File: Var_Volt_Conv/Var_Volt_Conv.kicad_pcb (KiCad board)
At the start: 6 copper layers, 114 x 120 mm, 98 parts, among them J101 Jack-DC, J102 Screw_Terminal_01x02, J103 Screw_Terminal_01x02, J201 Conn_01x05, Q101 AO3416, Q102 IRFML8244TRPBF, Q103 IRFML8244TRPBF, Q104 AO3407, Q105 AO3407, Q106 AO3407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

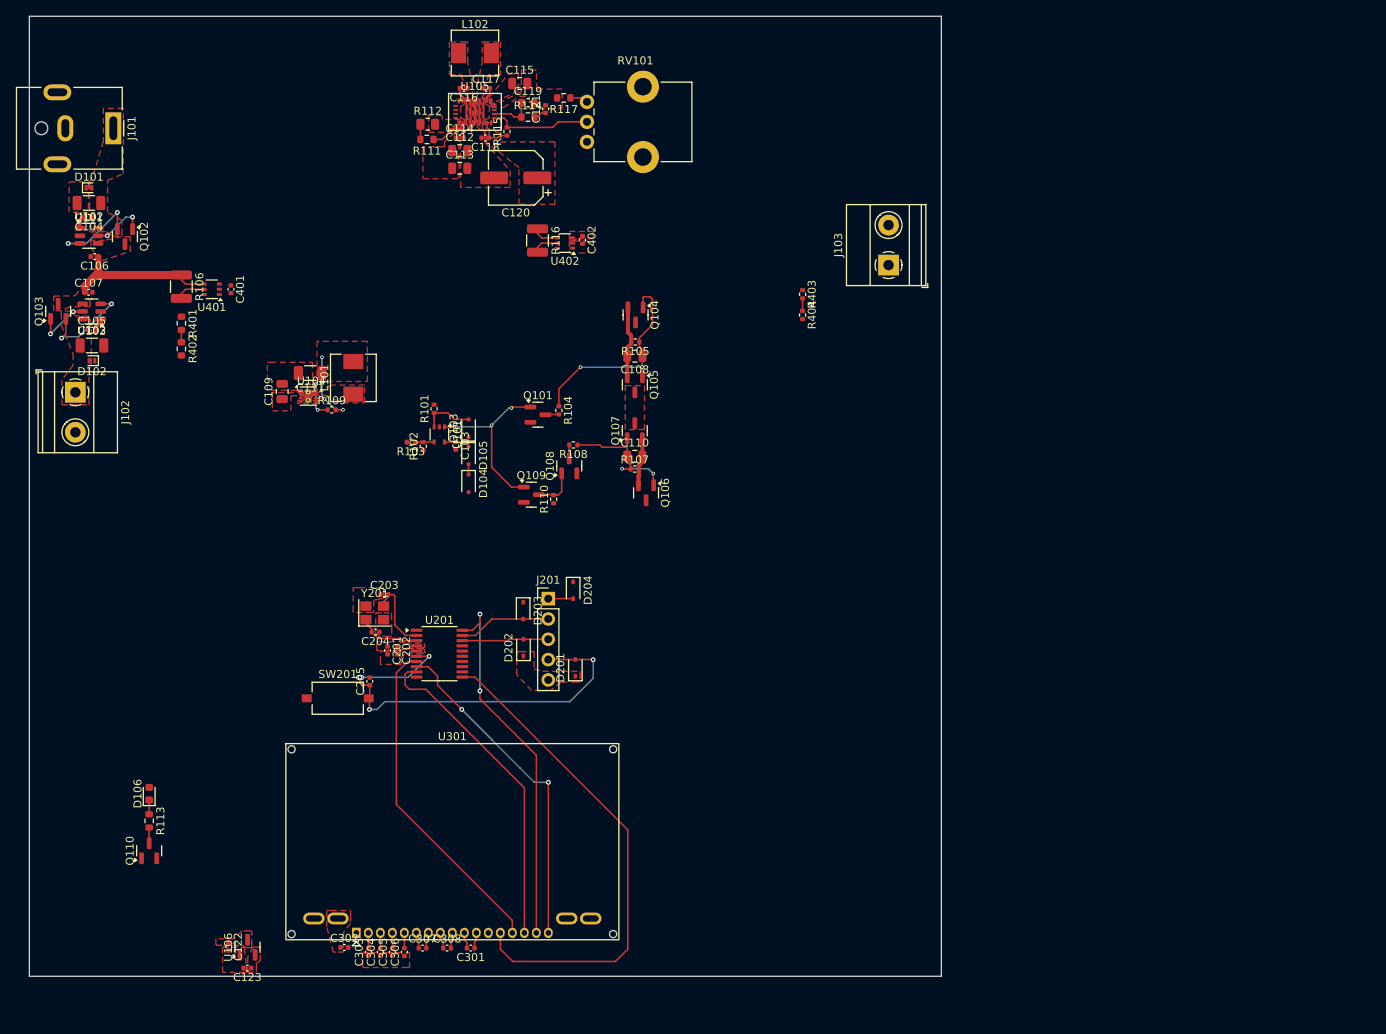
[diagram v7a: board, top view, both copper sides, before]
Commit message: Rounded PCB corners and add remaining 3D models
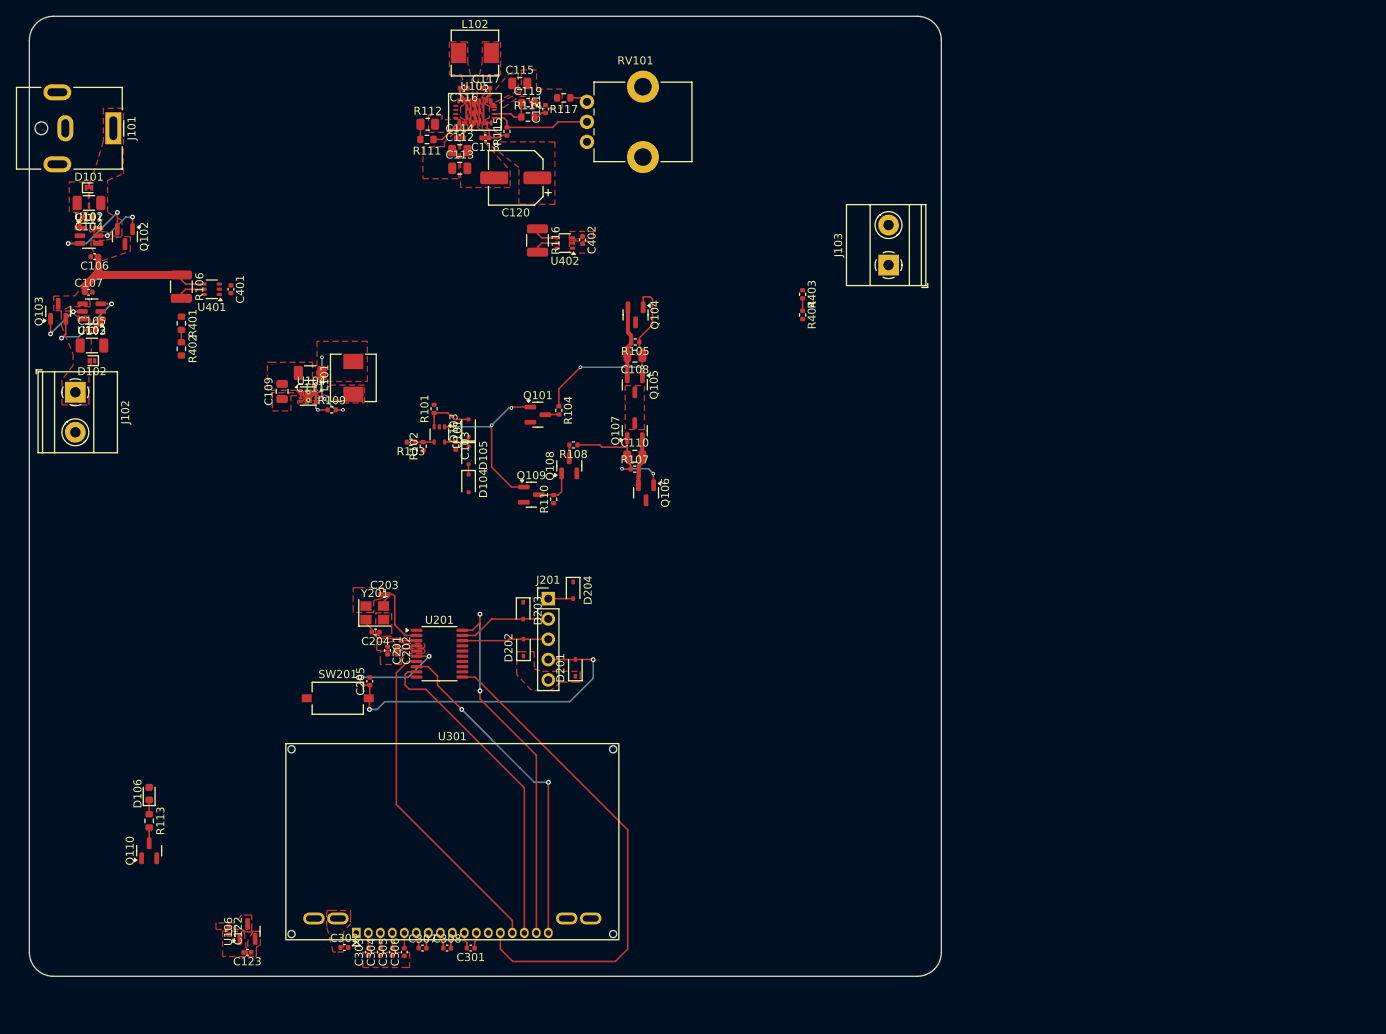
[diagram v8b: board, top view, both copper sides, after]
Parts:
- moved C122 1.98 mm to (44.9, 134.3)
- moved C123 1.97 mm to (47.2, 137.0)
- moved U106 1.97 mm to (47.3, 134.4)
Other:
- outline, holes or cut-outs redrawn
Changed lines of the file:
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@@
 			(remove_unused_layers no)
 		)
-		(model "${KICAD8_3DMODEL_DIR}/Display.3dshapes/NHD-C12832A1Z-FSRGB.wrl"
+		(model "${KIPRJMOD}/Project_Library/3d_Models/NHD-C12832A1Z.STEP"
 			(offset
-				(xyz 0 0 0)
+				(xyz 12 11.5 0)
 			)
 			(scale
@@
 	(footprint "Package_TO_SOT_SMD:SOT-23"
 		(layer "F.Cu")
-		(at 47.275 136.375 90)
+		(at 47.275 134.4 90)
 		(descr "SOT, 3 Pin (https://www.jedec.org/system/files/docs/to-236h.pdf variant AB), generated with kicad-footprint-generator ipc_gullwing_generator.py")
 		(tags "SOT TO_SOT_SMD")
@@
 		(tags "resistor")
 		(property "Reference" "R117"
-			(at 0 -1.43 360)
+			(at 0 -1.43 0)
 			(layer "F.SilkS")
 			(effects
@@
 		)
 		(property "Value" "6.4k"
-			(at 0 1.43 360)
+			(at 0 1.43 0)
 			(layer "F.Fab")
 			(effects
@@
 		)
 		(fp_text user "${REFERENCE}"
-			(at 0 0 360)
+			(at 0 0 0)
 			(layer "F.Fab")
 			(effects
@@
 			(pintype "passive")
 		)
-		(model "${KICAD8_3DMODEL_DIR}/Potentiometer_THT.3dshapes/Potentiometer_Bourns_PTV09A-1_Single_Vertical.wrl"
+		(model "${KIPRJMOD}/Project_Library/3d_Models/PTV09A-4225F-B104.step"
 			(offset
-				(xyz 0 0 0)
+				(xyz 7 2.5 0)
 			)
 			(scale
@@
 			)
 			(rotate
-				(xyz 0 0 0)
+				(xyz -90 0 90)
 			)
 		)
@@
 		(tags "SOT-363 SC-70-6")
 		(property "Reference" "U402"
-			(at 0 -2.25 360)
+			(at 0 -2.25 0)
 			(layer "F.SilkS")
 			(effects
@@
 		)
 		(property "Value" "INA215BIDCKR"
-			(at 0 2 360)
+			(at 0 2 0)
 			(layer "F.Fab")
 			(effects
@@
 		(tags "resistor")
 		(property "Reference" "R112"
-			(at 0 -1.65 360)
+			(at 0 -1.65 0)
 			(layer "F.SilkS")
 			(effects
@@
 		)
 		(property "Value" "4.3k"
-			(at 0 1.65 360)
+			(at 0 1.65 0)
 			(layer "F.Fab")
 			(effects
@@
 		)
 		(fp_text user "${REFERENCE}"
-			(at 0 0 360)
+			(at 0 0 0)
 			(layer "F.Fab")
 			(effects
@@
 		(tags "resistor")
 		(property "Reference" "R105"
-			(at 0 -1.17 360)
+			(at 0 -1.17 0)
 			(layer "F.SilkS")
 			(effects
@@
 		)
 		(property "Value" "100k"
-			(at 0 1.17 360)
+			(at 0 1.17 0)
 			(layer "F.Fab")
 			(effects
@@
 		)
 		(fp_text user "${REFERENCE}"
-			(at 0 0 360)
+			(at 0 0 0)
 			(layer "F.Fab")
 			(effects
@@
 	(footprint "Capacitor_SMD:C_0402_1005Metric"
 		(layer "F.Cu")
-		(at 47.25 138.975 180)
+		(at 47.25 137 180)
 		(descr "Capacitor SMD 0402 (1005 Metric), square (rectangular) end terminal, IPC_7351 nominal, (Body size source: IPC-SM-782 page 76, https://www.pcb-3d.com/wordpress/wp-content/uploads/ipc-sm-782a_amendment_1_and_2.pdf), generated with kicad-footprint-generator")
 		(tags "capacitor")
@@
 		(tags "capacitor")
 		(property "Reference" "C108"
-			(at 0 -1.68 360)
+			(at 0 -1.68 0)
 			(layer "F.SilkS")
 			(effects
@@
 		)
 		(property "Value" "10uF"
-			(at 0 1.68 360)
+			(at 0 1.68 0)
 			(layer "F.Fab")
 			(effects
@@
 		)
 		(fp_text user "${REFERENCE}"
-			(at 0 0 360)
+			(at 0 0 0)
 			(layer "F.Fab")
 			(effects
@@
 	(footprint "Capacitor_SMD:C_0402_1005Metric"
 		(layer "F.Cu")
-		(at 44.925 136.3 -90)
+		(at 44.925 134.325 -90)
 		(descr "Capacitor SMD 0402 (1005 Metric), square (rectangular) end terminal, IPC_7351 nominal, (Body size source: IPC-SM-782 page 76, https://www.pcb-3d.com/wordpress/wp-content/uploads/ipc-sm-782a_amendment_1_and_2.pdf), generated with kicad-footprint-generator")
 		(tags "capacitor")
@@
 		)
 	)
+	(gr_arc
+		(start 20 23)
+		(mid 20.87868 20.87868)
+		(end 23 20)
+		(stroke
+			(width 0.05)
+			(type default)
+		)
+		(layer "Edge.Cuts")
+	)
+	(gr_arc
+		(start 134 137)
+		(mid 133.12132 139.12132)
+		(end 131 140)
+		(stroke
+			(width 0.05)
+			(type default)
+		)
+		(layer "Edge.Cuts")
+	)
 	(gr_line
-		(start 134 140)
-		(end 20 140)
+		(start 131 140)
+		(end 23 140)
+		(stroke
+			(width 0.05)
+			(type default)
+		)
+		(layer "Edge.Cuts")
+	)
+	(gr_arc
+		(start 23 140)
+		(mid 20.87868 139.12132)
+		(end 20 137)
+		(stroke
+			(width 0.05)
+			(type default)
+		)
+		(layer "Edge.Cuts")
+	)
+	(gr_arc
+		(start 131 20)
+		(mid 133.12132 20.87868)
+		(end 134 23)
 		(stroke
 			(width 0.05)
@@
 	)
 	(gr_line
-		(start 134 20)
-		(end 134 140)
+		(start 134 23)
+		(end 134 137)
 		(stroke
 			(width 0.05)
@@
 	)
 	(gr_line
-		(start 20 20)
-		(end 134 20)
+		(start 23 20)
+		(end 131 20)
 		(stroke
 			(width 0.05)
@@
 	)
 	(gr_line
-		(start 20 140)
-		(end 20 20)
+		(start 20 137)
+		(end 20 23)
 		(stroke
 			(width 0.05)
@@
 		(polygon
 			(pts
-				(xy 44.15 136.35) (xy 46.875 136.35) (xy 46.875 136.525) (xy 47.125 138.7) (xy 47.125 139.525) (xy 46.95 139.525)
-				(xy 44.575 139.5) (xy 44.325 139.5) (xy 44.15 139.5) (xy 44.15 136.475)
+				(xy 44.15 134.375) (xy 46.875 134.375) (xy 46.875 134.55) (xy 47.125 136.725) (xy 47.125 137.55)
+				(xy 46.95 137.55) (xy 44.575 137.525) (xy 44.325 137.525) (xy 44.15 137.525) (xy 44.15 134.5)
 			)
 		)
@@
 		(polygon
 			(pts
-				(xy 46.6 136.125) (xy 47.05 136.425) (xy 47.8 136.425) (xy 47.8 136.125) (xy 47.8 134.325) (xy 47.55 134.325)
-				(xy 46.575 134.325) (xy 45.6 135.3) (xy 43.325 135.3) (xy 43.325 135.5) (xy 43.325 136) (xy 43.325 136.125)
-				(xy 44.3 136.125)
+				(xy 46.6 134.15) (xy 47.05 134.45) (xy 47.8 134.45) (xy 47.8 134.15) (xy 47.8 132.35) (xy 47.55 132.35)
+				(xy 46.575 132.35) (xy 45.6 133.325) (xy 43.325 133.325) (xy 43.325 133.525) (xy 43.325 134.025)
+				(xy 43.325 134.15) (xy 44.3 134.15)
 			)
 		)
@@
 		(polygon
 			(pts
-				(xy 47.3 139.5) (xy 48.375 139.5) (xy 48.375 139.15) (xy 48.375 138.375) (xy 48.875 138.05) (xy 48.875 136.35)
-				(xy 48.65 136.35) (xy 47.975 136.35) (xy 47.35 137.475) (xy 47.3 137.6) (xy 47.3 139.425)
+				(xy 47.3 137.525) (xy 48.375 137.525) (xy 48.375 137.175) (xy 48.375 136.4) (xy 48.875 136.075)
+				(xy 48.875 134.375) (xy 48.65 134.375) (xy 47.975 134.375) (xy 47.35 135.5) (xy 47.3 135.625) (xy 47.3 137.45)
 			)
 		)
